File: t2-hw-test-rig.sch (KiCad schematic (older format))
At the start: 10 parts

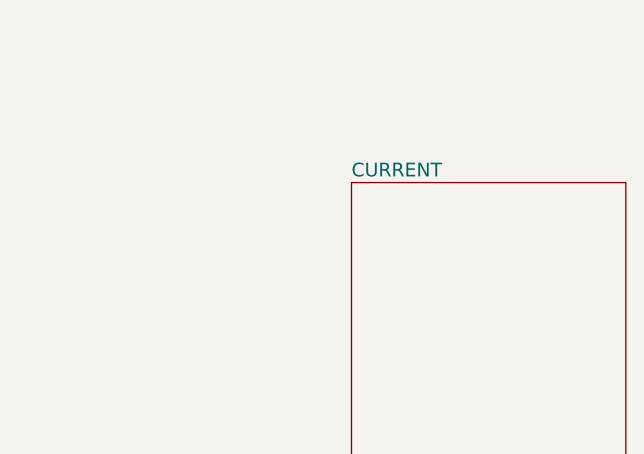
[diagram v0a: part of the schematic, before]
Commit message: pin allocations and finally got the opamp in there
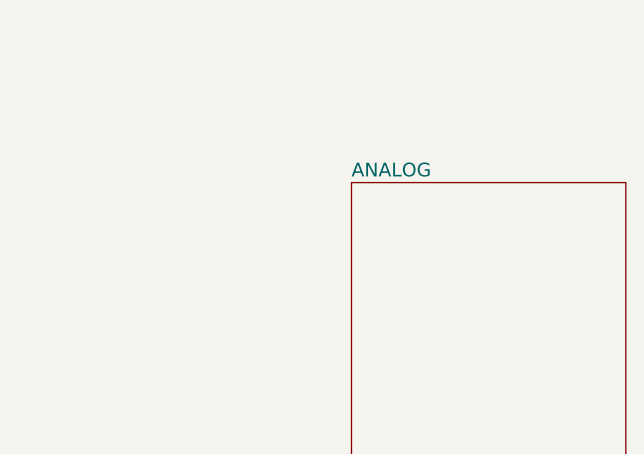
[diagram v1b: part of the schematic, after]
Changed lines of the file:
@@
 S 7500 3300 1200 1200
 U 55375CFB
-F0 "CURRENT" 60
+F0 "ANALOG" 60
 F1 "current.sch" 60
 $EndSheet

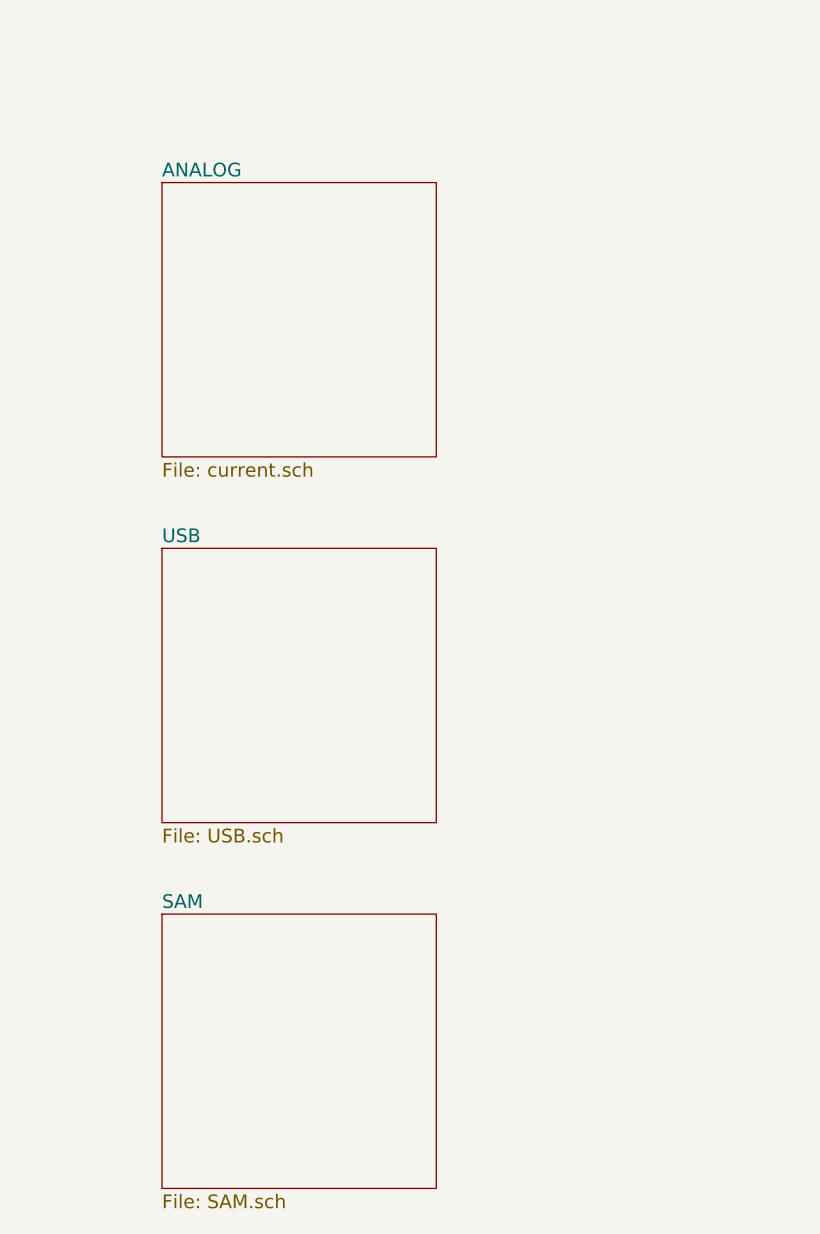
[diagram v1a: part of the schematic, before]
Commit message: connected analog things, lots of testpoints
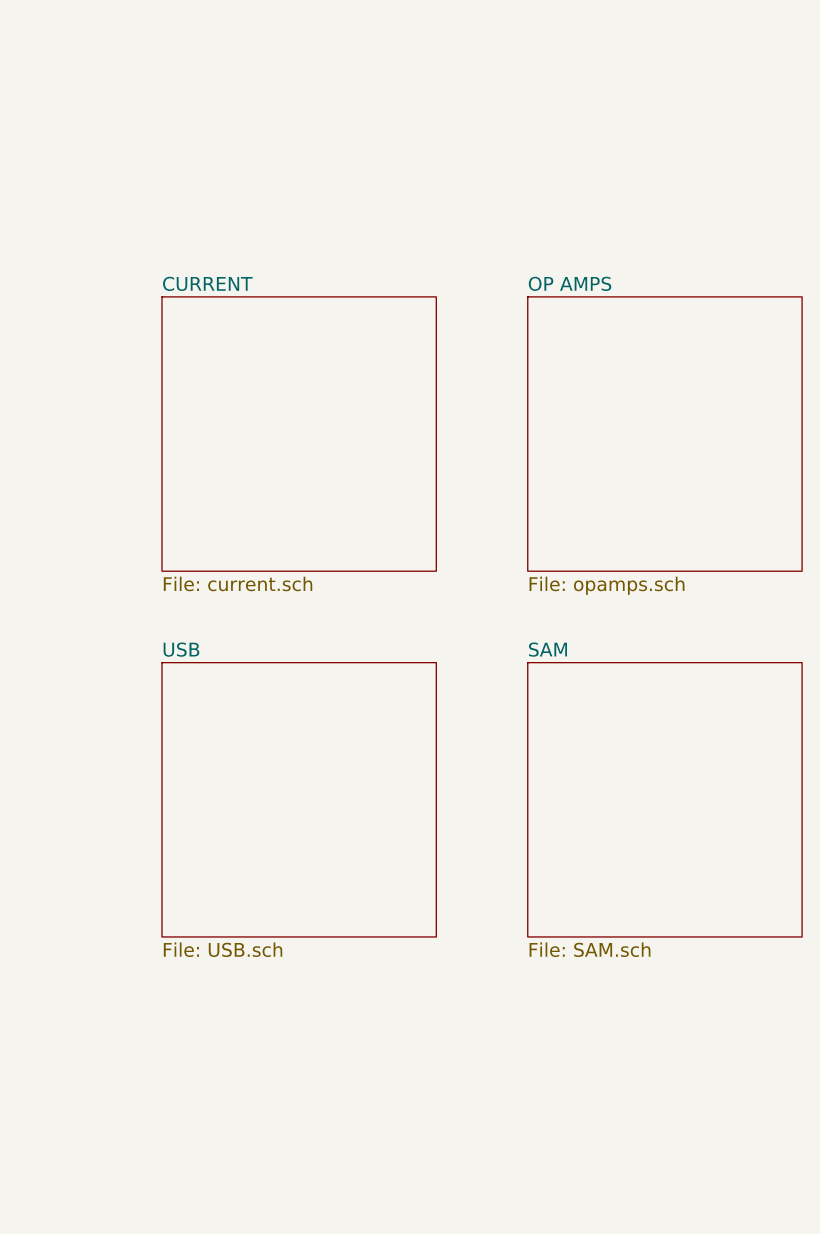
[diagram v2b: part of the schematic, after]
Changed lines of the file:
@@
 $Descr B 17000 11000
 encoding utf-8
-Sheet 1 4
+Sheet 1 5
 Title "Tessel 2 Test Rig"
 Date "Thu 16 Apr 2015"
@@
 $EndComp
 $Sheet
-S 7500 4900 1200 1200
+S 7500 5400 1200 1200
 U 55373628
 F0 "USB" 60
@@
 $EndSheet
 $Sheet
-S 7500 6500 1200 1200
+S 9100 5400 1200 1200
 U 5537389A
 F0 "SAM" 60
@@
 $EndSheet
 $Sheet
-S 7500 3300 1200 1200
+S 7500 3800 1200 1200
 U 55375CFB
-F0 "ANALOG" 60
+F0 "CURRENT" 60
 F1 "current.sch" 60
 $EndSheet
@@
 Text Notes 5000 4600 0    60   ~ 0
 3.3V LDO
+$Sheet
+S 9100 3800 1200 1200
+U 55403272
+F0 "OP AMPS" 60
+F1 "opamps.sch" 60
+$EndSheet
 $EndSCHEMATC

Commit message: passed schematic review
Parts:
- added H? (x4): M2.5, symbol HOLE
- added J?: CONN_01X02, symbol CONN_01X02
- added JP?: JUMPER, symbol JUMPER
- added MP? (x4): 98952A202, symbol MECHANICAL
- added MP? (x4): 98952A209, symbol MECHANICAL
- added MP?: PLATE, symbol MECHANICAL
- added MP? (x4): 92290A060, symbol MECHANICAL
- added MP?: 201B, symbol MECHANICAL
- added P? (x2): USB A TO MicroUSB A CABLE, symbol CONN_01X04
- added P?: ETHERNET CABLE, symbol CONN_01X08
- added P?: 5VDC POWER, symbol CONN_01X02
- added P? (x2): USB THUMB DRIVE, symbol CONN_01X04
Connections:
- net +5V: now also J?.2 (P2)
- net V_IN: now also J?.1 (P1)
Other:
- note added: "1/4" ACRYLIC, LASER CUT MOUNTING PLATE"
- note added: "5V POWER CABLE/BARREL PLUG\nFROM\nEXTERNAL POWER SUPPLY\nTO\nTEST RIG"
- note added: "ADDITIONAL HARDWARE\nMAY BE NECESSARY FOR\nTOGGLE CLAMP MOUNTING"
- note added: "ALL TESTPOINTS ARE POGO PINS\nTO UUT UNLESS OTHERWISE SPECIFIED"
- note added: "LAN\nFROM\nUPSTREAM SWITCH\nTO\nUUT"
- note added: "M2.5 x 10mm SHCS"
- note added: "M2.5 x 10mm STANDOFF"
- note added: "M2.5 x 5mm STANDOFF"
- note added: "MISC. USB DEVICES\nTO\nUUT\nFOR\nUSB I/O TESTS"
- note added: "RIG STACKUP/ASSEMBLY:"
- note added: "TEST RIG PCB MOUNT HOLES"
- note added: "TOGGLE CLAMP ASSEMBLY"
- note added: "USB\nFROM\nTEST RIG\nTO\nUUT"
- note added: "USB\nFROM\nUPSTREAM MASTER\nTO\nTEST RIG"
- note added: "UUT"
